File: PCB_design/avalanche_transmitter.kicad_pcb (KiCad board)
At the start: 2 copper layers, 55 x 110 mm, 27 parts

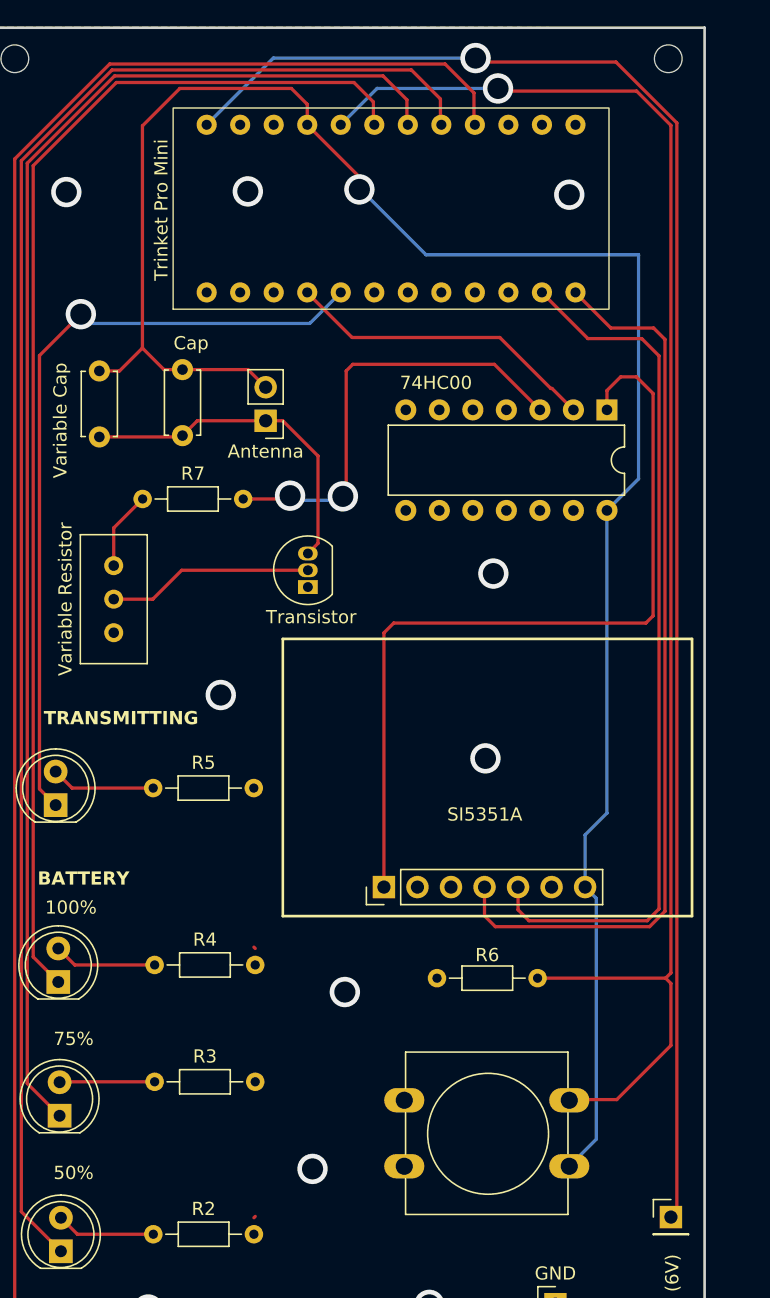
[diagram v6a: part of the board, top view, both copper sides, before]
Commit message: adjusted pin connectors on PCB to lead to vias with red wires
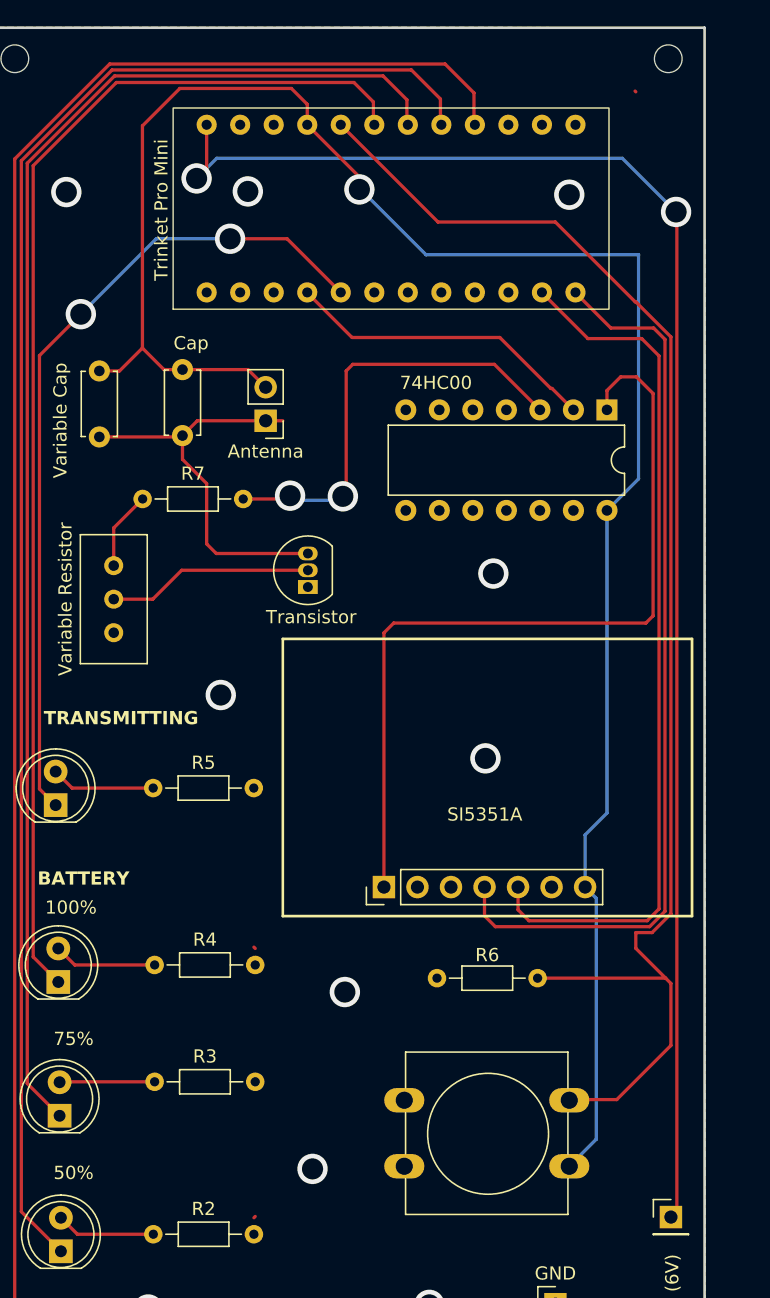
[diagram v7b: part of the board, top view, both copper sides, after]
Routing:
- net Net-(U2-8): track 116.6 -> 107.7 mm, vias 1 -> 0
- net Net-(Q1-C): track 25.9 -> 31.3 mm
- net Net-(D5-K): track 59.9 -> 63.5 mm, vias 1 -> 2
- net +6V: track 122.6 -> 119.4 mm, vias 1 -> 2
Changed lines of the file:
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@@
   )
   (segment (start 47.6 46) (end 47.7 45.9) (width 0.25) (layer "F.Cu") (net 1))
+  (segment (start 49.53 49.53) (end 49.53 54.102) (width 0.25) (layer "F.Cu") (net 1))
   (segment (start 47.7 45.9) (end 48.825 44.775) (width 0.25) (layer "F.Cu") (net 1))
+  (segment (start 50.258 54.83) (end 57.2 54.83) (width 0.25) (layer "F.Cu") (net 1))
+  (segment (start 47.7 45.9) (end 47.7 47.7) (width 0.25) (layer "F.Cu") (net 1))
+  (segment (start 49.53 54.102) (end 50.258 54.83) (width 0.25) (layer "F.Cu") (net 1))
   (segment (start 41.4 46) (end 47.6 46) (width 0.25) (layer "F.Cu") (net 1))
-  (segment (start 57.965 54.065) (end 57.965 47.439034) (width 0.25) (layer "F.Cu") (net 1))
-  (segment (start 57.2 54.83) (end 57.965 54.065) (width 0.25) (layer "F.Cu") (net 1))
   (segment (start 55.300966 44.775) (end 54 44.775) (width 0.25) (layer "F.Cu") (net 1))
-  (segment (start 57.965 47.439034) (end 55.300966 44.775) (width 0.25) (layer "F.Cu") (net 1))
   (segment (start 48.825 44.775) (end 54 44.775) (width 0.25) (layer "F.Cu") (net 1))
+  (segment (start 47.7 47.7) (end 49.53 49.53) (width 0.25) (layer "F.Cu") (net 1))
   (segment (start 47.7 40.9) (end 52.665 40.9) (width 0.25) (layer "F.Cu") (net 2))
   (segment (start 47.5 19.6) (end 55.95 19.6) (width 0.25) (layer "F.Cu") (net 2))
@@
   (segment (start 39.54 86) (end 38.29 84.75) (width 0.25) (layer "F.Cu") (net 10))
   (segment (start 45.59 86) (end 39.54 86) (width 0.25) (layer "F.Cu") (net 10))
+  (segment (start 59.69 35.052) (end 55.626 30.988) (width 0.25) (layer "F.Cu") (net 11))
+  (segment (start 55.626 30.988) (end 51.562 30.988) (width 0.25) (layer "F.Cu") (net 11))
   (segment (start 36.865 72.665) (end 36.865 39.835) (width 0.25) (layer "F.Cu") (net 11))
   (segment (start 38.09 73.89) (end 36.865 72.665) (width 0.25) (layer "F.Cu") (net 11))
   (segment (start 36.865 39.835) (end 40 36.7) (width 0.25) (layer "F.Cu") (net 11))
+  (via (at 51.308 30.988) (size 2.3) (drill 1.6) (layers "F.Cu" "B.Cu") (net 11))
   (via (at 40 36.7) (size 2.3) (drill 1.6) (layers "F.Cu" "B.Cu") (net 11))
-  (segment (start 57.342 37.4) (end 59.69 35.052) (width 0.25) (layer "B.Cu") (net 11))
-  (segment (start 40.7 37.4) (end 57.342 37.4) (width 0.25) (layer "B.Cu") (net 11))
+  (segment (start 51.308 30.988) (end 45.712 30.988) (width 0.25) (layer "B.Cu") (net 11))
+  (segment (start 45.712 30.988) (end 40 36.7) (width 0.25) (layer "B.Cu") (net 11))
   (segment (start 40 36.7) (end 40.7 37.4) (width 0.25) (layer "B.Cu") (net 11))
   (segment (start 45.48 72.6) (end 39.34 72.6) (width 0.25) (layer "F.Cu") (net 12))
   (segment (start 39.34 72.6) (end 38.09 71.35) (width 0.25) (layer "F.Cu") (net 12))
+  (segment (start 84.7 82.122792) (end 84.7 38.423604) (width 0.25) (layer "F.Cu") (net 13))
+  (segment (start 82.042 84.742) (end 82.042 83.55) (width 0.25) (layer "F.Cu") (net 13))
   (segment (start 74.6 87) (end 84.3 87) (width 0.25) (layer "F.Cu") (net 13))
-  (segment (start 84.7 22.4) (end 82.1 19.8) (width 0.25) (layer "F.Cu") (net 13))
-  (segment (start 82.1 19.8) (end 71.7 19.8) (width 0.25) (layer "F.Cu") (net 13))
   (segment (start 80.6 96.2) (end 76.7 96.2) (width 0.25) (layer "F.Cu") (net 13))
   (segment (start 84.7 87.4) (end 84.7 92.1) (width 0.25) (layer "F.Cu") (net 13))
-  (segment (start 84.7 86.6) (end 84.7 22.4) (width 0.25) (layer "F.Cu") (net 13))
+  (segment (start 82.042 83.55) (end 83.272792 83.55) (width 0.25) (layer "F.Cu") (net 13))
+  (segment (start 67.056 29.718) (end 75.946 29.718) (width 0.25) (layer "F.Cu") (net 13))
+  (segment (start 59.69 22.352) (end 67.056 29.718) (width 0.25) (layer "F.Cu") (net 13))
+  (segment (start 75.946 29.718) (end 81.993604 35.765604) (width 0.25) (layer "F.Cu") (net 13))
   (segment (start 84.7 92.1) (end 80.6 96.2) (width 0.25) (layer "F.Cu") (net 13))
   (segment (start 84.3 87) (end 84.7 87.4) (width 0.25) (layer "F.Cu") (net 13))
-  (segment (start 84.3 87) (end 84.7 86.6) (width 0.25) (layer "F.Cu") (net 13))
-  (via (at 71.6 19.6) (size 2.3) (drill 1.6) (layers "F.Cu" "B.Cu") (net 13))
-  (segment (start 71.6 19.6) (end 62.442 19.6) (width 0.25) (layer "B.Cu") (net 13))
-  (segment (start 62.442 19.6) (end 59.69 22.352) (width 0.25) (layer "B.Cu") (net 13))
+  (segment (start 83.272792 83.55) (end 84.7 82.122792) (width 0.25) (layer "F.Cu") (net 13))
+  (segment (start 84.3 87) (end 82.042 84.742) (width 0.25) (layer "F.Cu") (net 13))
+  (segment (start 82.042 19.858) (end 81.984 19.8) (width 0.25) (layer "F.Cu") (net 13))
+  (segment (start 84.7 38.423604) (end 82.042 35.765604) (width 0.25) (layer "F.Cu") (net 13))
+  (segment (start 81.993604 35.765604) (end 82.042 35.765604) (width 0.25) (layer "F.Cu") (net 13))
   (segment (start 75.601 42.327) (end 71.74 38.466) (width 0.25) (layer "F.Cu") (net 14))
   (segment (start 77.315 43.95) (end 75.692 42.327) (width 0.25) (layer "F.Cu") (net 14))
@@
   (segment (start 71.74 38.466) (end 60.546 38.466) (width 0.25) (layer "F.Cu") (net 14))
   (segment (start 60.546 38.466) (end 57.08 35) (width 0.25) (layer "F.Cu") (net 14))
-  (segment (start 84.7 105.1) (end 85.15 104.65) (width 0.25) (layer "F.Cu") (net 15))
-  (segment (start 85.15 22.213604) (end 80.536396 17.6) (width 0.25) (layer "F.Cu") (net 15))
-  (segment (start 80.536396 17.6) (end 70 17.6) (width 0.25) (layer "F.Cu") (net 15))
-  (segment (start 85.15 104.65) (end 85.15 22.213604) (width 0.25) (layer "F.Cu") (net 15))
-  (via (at 69.9 17.3) (size 2.3) (drill 1.6) (layers "F.Cu" "B.Cu") (net 15))
-  (segment (start 69.9 17.3) (end 54.582 17.3) (width 0.25) (layer "B.Cu") (net 15))
-  (segment (start 54.582 17.3) (end 49.53 22.352) (width 0.25) (layer "B.Cu") (net 15))
+  (segment (start 48.768 26.416) (end 49.53 25.654) (width 0.25) (layer "F.Cu") (net 15))
+  (segment (start 85.15 104.65) (end 84.7 105.1) (width 0.25) (layer "F.Cu") (net 15))
+  (segment (start 49.53 25.654) (end 49.53 22.352) (width 0.25) (layer "F.Cu") (net 15))
+  (segment (start 85.15 29.016) (end 85.15 104.65) (width 0.25) (layer "F.Cu") (net 15))
+  (segment (start 85.09 28.956) (end 85.15 29.016) (width 0.25) (layer "F.Cu") (net 15))
+  (via (at 48.768 26.416) (size 2.3) (drill 1.6) (layers "F.Cu" "B.Cu") (net 15))
+  (via (at 85.09 28.956) (size 2.3) (drill 1.6) (layers "F.Cu" "B.Cu") (net 15))
+  (segment (start 48.768 26.416) (end 50.292 24.892) (width 0.25) (layer "B.Cu") (net 15))
+  (segment (start 50.292 24.892) (end 81.026 24.892) (width 0.25) (layer "B.Cu") (net 15))
+  (segment (start 81.026 24.892) (end 85.09 28.956) (width 0.25) (layer "B.Cu") (net 15))
   (segment (start 83.35 42.71) (end 83.35 59.55) (width 0.25) (layer "F.Cu") (net 16))
   (segment (start 82.8 60.1) (end 63.7 60.1) (width 0.25) (layer "F.Cu") (net 16))

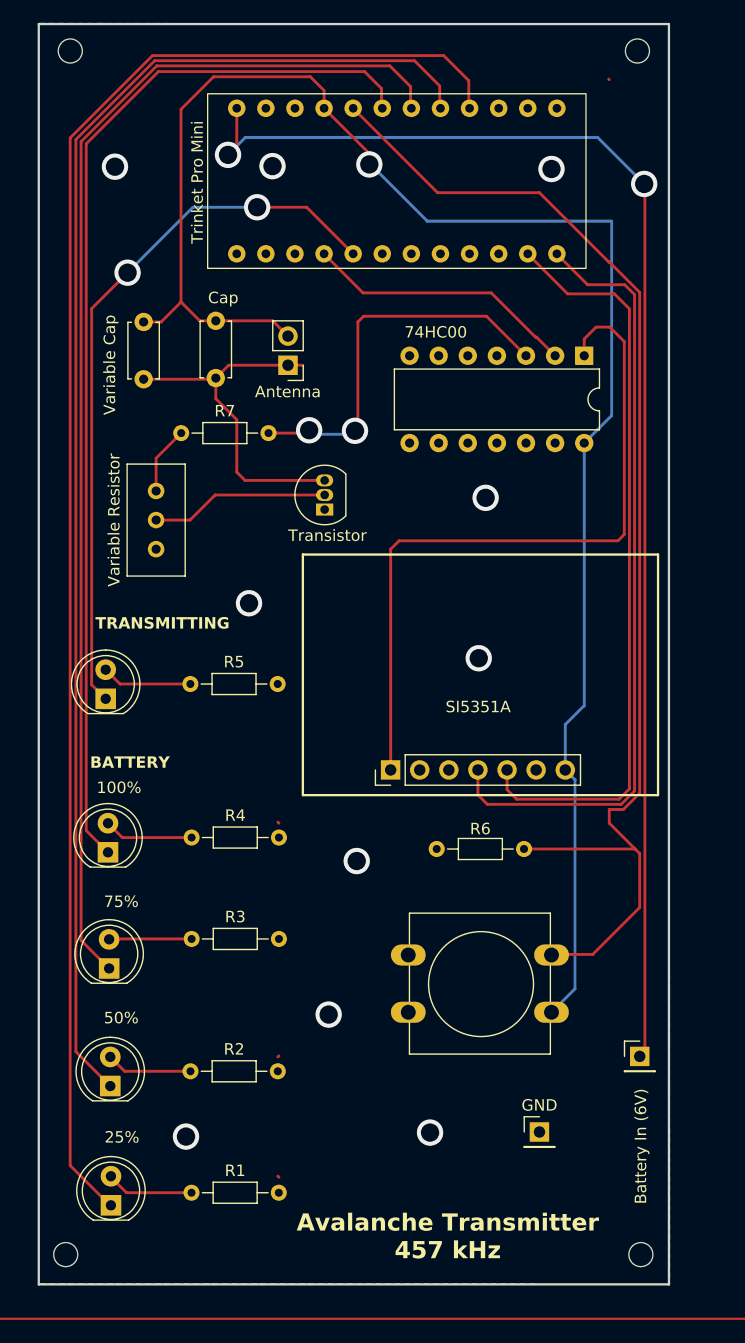
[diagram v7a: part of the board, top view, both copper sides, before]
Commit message: Changes ben recommended made
added on/off switch
added resistor in series with antenna
swapped LEDs to correct direction
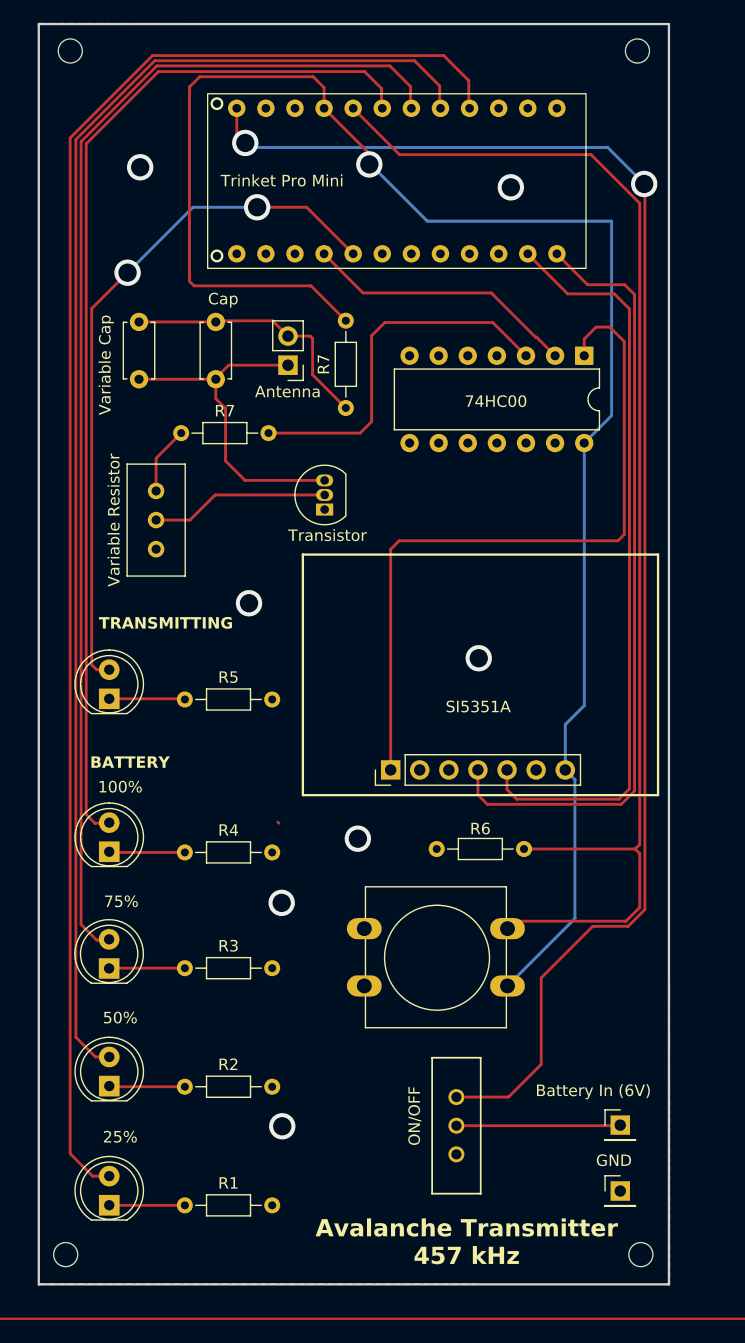
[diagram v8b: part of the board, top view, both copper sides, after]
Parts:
- added ON/OFF: SW_1218_EWI, SW_1218_EWI:SW_1218_EWI, F.Cu at (68.7, 108.7)
- added R7: R_Small, Resistor_THT:R_Axial_DIN0204_L3.6mm_D1.6mm_P7.62mm_Horizontal, F.Cu at (59.0, 48.5)
- moved GND 8.73 mm to (83.0, 116.8)
- moved Battery In (6V) 6.24 mm to (83.0, 111.1)
- moved REF** 4.48 mm to (60.7, 94.0)
- moved R3 2.62 mm to (45.0, 97.4)
- moved R2 1.44 mm to (45.0, 107.8)
- moved R5 1.43 mm to (45.0, 74.0)
- moved R4 1.43 mm to (45.0, 87.3)
- moved R1 1.24 mm to (45.0, 118.1)
- moved Variable Cap 0.40 mm to (41.0, 41.0)
- moved TRANSMITTING 0.31 mm to (38.4, 73.9)
- moved 25% 0.15 mm to (38.4, 118.1)
- moved 100% 0.12 mm to (38.4, 87.2)
- moved Cap 0.10 mm to (47.7, 41.0)
- moved 50% 0.09 mm to (38.4, 107.7)
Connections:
- 100% pad 1: Net-(D1-K) -> Net-(D4-A)
- 100% pad 2: Net-(D4-A) -> Net-(D1-K)
- 25% pad 1: Net-(D4-K) -> Net-(D1-A)
- 25% pad 2: Net-(D1-A) -> Net-(D4-K)
- 50% pad 1: Net-(D3-K) -> Net-(D2-A)
- 50% pad 2: Net-(D2-A) -> Net-(D3-K)
- 75% pad 1: Net-(D2-K) -> Net-(D3-A)
- 75% pad 2: Net-(D3-A) -> Net-(D2-K)
- TRANSMITTING pad 1: Net-(D5-K) -> Net-(D5-A)
- TRANSMITTING pad 2: Net-(D5-A) -> Net-(D5-K)
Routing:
- net +6V: track 119.4 -> 145.0 mm
- net +3V0: track 148.8 -> 170.4 mm
- net Net-(U2-8): track 107.7 -> 112.2 mm
- net Net-(D5-K): track 63.5 -> 60.4 mm
- net Net-(D4-K): track 135.8 -> 133.9 mm
- net Net-(D1-K): track 93.3 -> 91.4 mm
- net Net-(D2-K): track 107.3 -> 105.5 mm
- net Net-(D3-K): track 121.3 -> 119.5 mm
- net Net-(R7-Pad2): track 33.8 -> 32.1 mm, vias 2 -> 0
- net Net-(Q1-C): track 31.3 -> 30.0 mm
- net Net-(D5-A): track 7.91 -> 6.93 mm
- net Net-(D1-A): track 7.53 -> 6.60 mm
- net Net-(D2-A): track 7.52 -> 6.92 mm
- net Net-(D4-A): track 7.82 -> 7.24 mm
- net GND: track 0.42 -> 0.14 mm, vias 10 -> 7
